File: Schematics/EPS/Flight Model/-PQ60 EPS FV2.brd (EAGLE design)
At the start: 42 x 42 mm, 58 parts, among them U1 LTC3105EDDPBF, U10 INA3221AIRGVT, U2 LTC3105EDDPBF, U3 LTC3105EDDPBF, U4 LTC4413EDDPBF, U5 LTC4413EDDPBF, U6 TPS63001DRCR, U7 TPS2552DBVT, U8 TPS2552DBVT

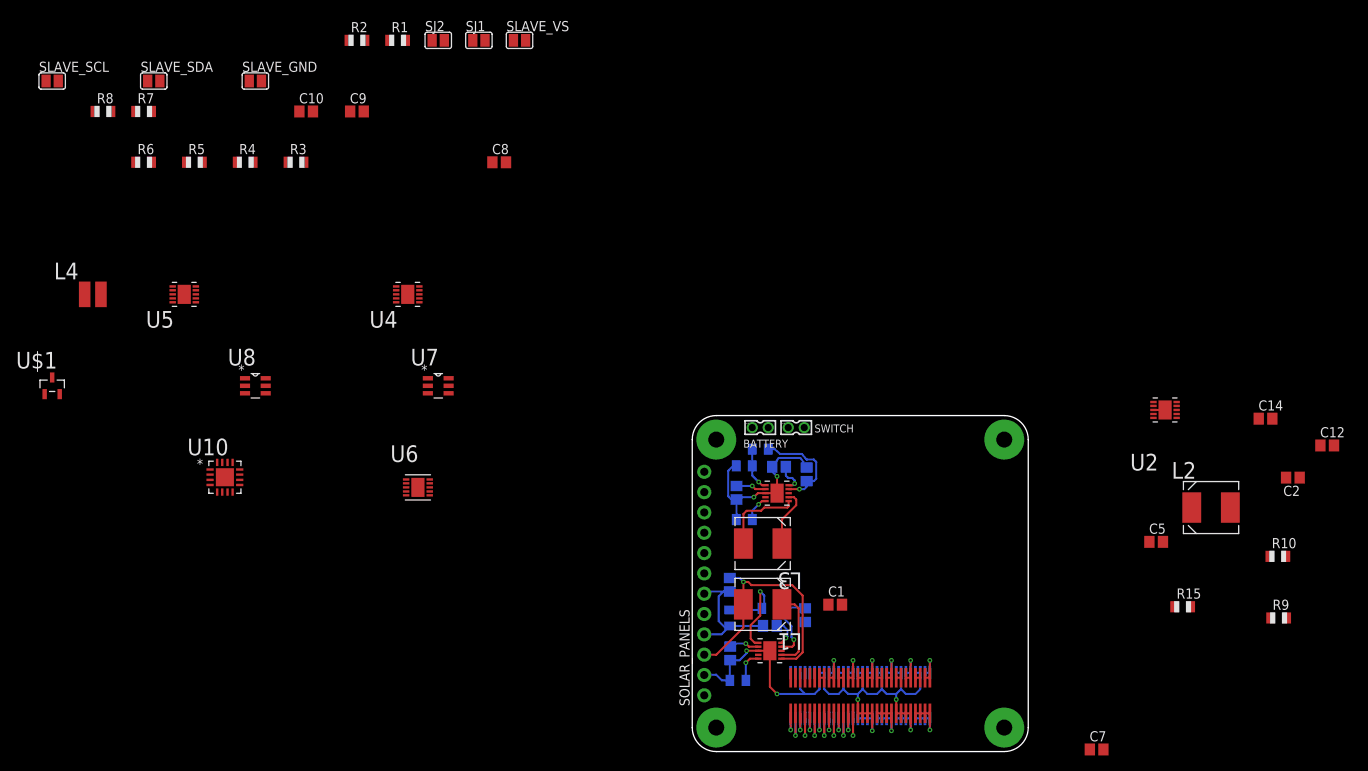
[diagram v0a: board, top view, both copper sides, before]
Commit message: Complteded routing
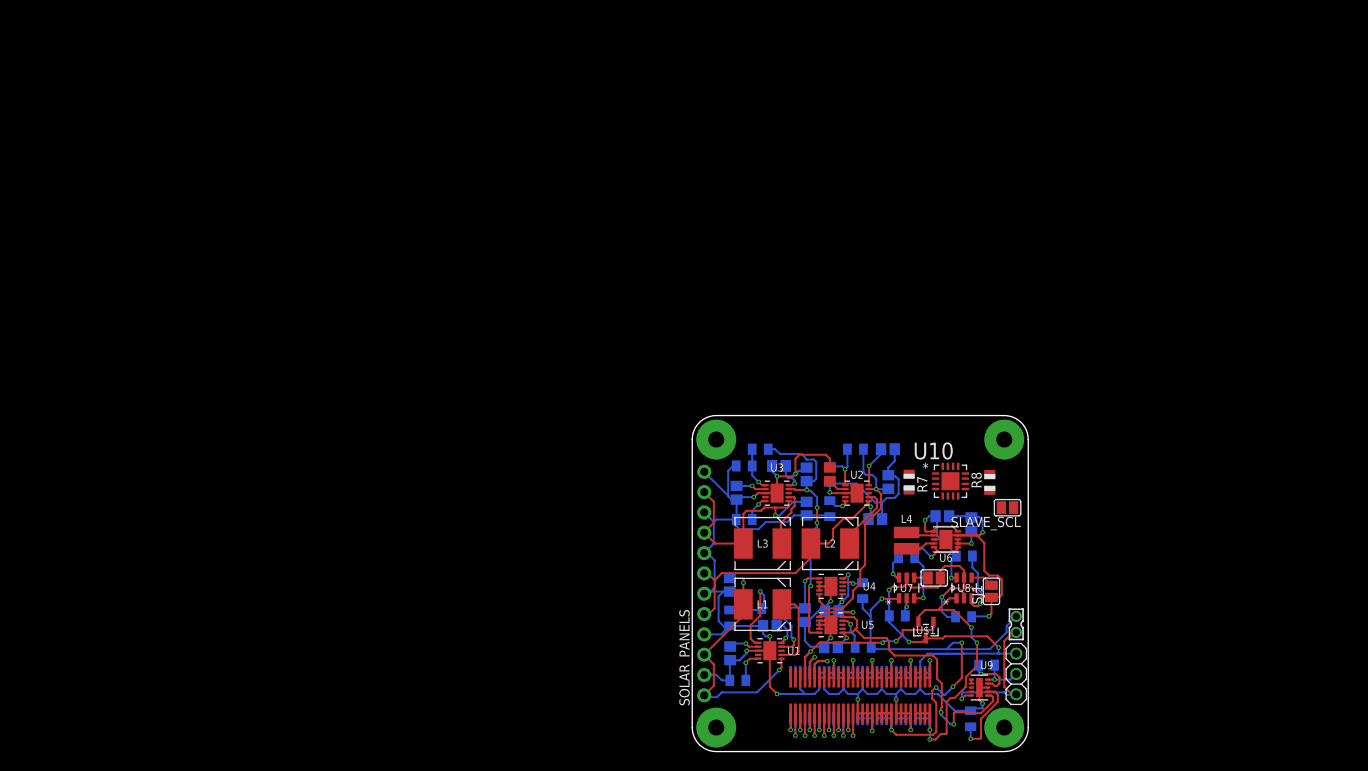
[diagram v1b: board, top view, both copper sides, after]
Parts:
- removed SLAVE_GND, SLAVE_SDA, SLAVE_VS: (no value), jumper:SJ
- added R18: 487, adafruit:R0805
- added R19: (no value), adafruit:R0805
- added U9: BQ24210DQCT, BQ24210:SON50P200X300X80-11N
- BATTERY: value 332-02 -> (none); device con-garry:332-02 -> adafruit:1X03
- R1, R2: value (none) -> 470k
- moved SLAVE_SCL 130.8 mm to (39.4, 30.5), turned to 180 degrees
- moved R8 120.2 mm to (37.2, 33.6), turned to 90 degrees
- moved R6 113.8 mm to (34.0, 24.4), flipped to the bottom, turned to 180 degrees
- moved U$1 113.4 mm to (29.2, 15.2), turned to 180 degrees
- moved R7 106.3 mm to (27.1, 33.7), turned to 270 degrees
- moved L4 106.3 mm to (26.8, 26.4), turned to 90 degrees
- moved R4 106.3 mm to (33.9, 16.8), flipped to the bottom, turned to 180 degrees
- moved R5 101.8 mm to (26.8, 24.2), flipped to the bottom, turned to 180 degrees
- moved R1 95.6 mm to (21.4, 13.0), flipped to the bottom, turned to 180 degrees
- moved C10 94.3 mm to (31.3, 29.4), flipped to the bottom
- moved R3 94.1 mm to (25.6, 17.0), flipped to the bottom
- moved SJ1 94.1 mm to (37.4, 20.0), turned to 90 degrees
- moved R2 93.4 mm to (21.3, 20.1), flipped to the bottom, turned to 270 degrees
- moved C9 92.5 mm to (34.9, 28.4), flipped to the bottom, turned to 270 degrees
- moved U8 92.1 mm to (34.0, 20.4), turned to 90 degrees
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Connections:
- removed net $N70: BATTERY.1, C8.2, SWITCH.1, U5.10, U5.6
- new net N$31: C8.2, U5.10, U5.6, U9.1
- new net N$32: U9.6, U9.7
- new net N$33: R18.2, U9.2
- new net N$34: BATTERY.1, SWITCH.1, U9.10
- new net N$35: BATTERY.2, R19.2, U9.5
- new net N$36: R19.1, U9.4
- net !RST: now also U$3.P$27
- net +3V3: no longer SLAVE_VS.1
- net BATV: now also SWITCH.2
- net GND: now also BATTERY.3, R18.1, U9.3; no longer BATTERY.2, SLAVE_GND.1
- net GPIO0: now also U$3.P$25
- net GPIO1: now also U$3.P$26
- net I2C_SDA: no longer SLAVE_SDA.1
- net N$18: no longer SLAVE_GND.2, SLAVE_SDA.2, SLAVE_VS.2
- net SCL: now also U$3.P$29
- net SDA: now also U$3.P$30
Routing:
- net GND: track 121.1 -> 313.3 mm, vias 8 -> 19
- net BATV: track 7.32 -> 63.9 mm, vias 1 -> 5
- net N$31: track 0.00 -> 37.5 mm, vias 0 -> 3
- net PANEL3+4: track 0.00 -> 34.4 mm, vias 0 -> 1
- net +3V3: track 7.13 -> 37.9 mm, vias 1 -> 4
- net N$6: track 0.00 -> 29.9 mm, vias 0 -> 1
- net !RST: track 0.00 -> 24.2 mm, vias 0 -> 3
- net N$7: track 13.2 -> 33.7 mm, vias 1 -> 4
- net N$34: track 0.00 -> 18.6 mm, vias 0 -> 1
- net BATTERY: track 0.00 -> 17.7 mm, vias 0 -> 3
- net UNPROTECTED3V3: track 0.00 -> 17.3 mm, vias 0 -> 2
- net PANEL5+6: track 10.4 -> 27.6 mm, vias 0 -> 1
- net N$9: track 0.00 -> 13.3 mm, vias 0 -> 3
- net N$33: track 0.00 -> 10.6 mm, vias 0 -> 1
- net N$15: track 0.00 -> 8.52 mm, vias 0 -> 1
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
